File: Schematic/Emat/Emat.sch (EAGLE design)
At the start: 32 parts, among them J1 PIN1-2, J2 PIN1-2, J3 PIN1-2, J4 PIN1-2, Q2 STP13NM60N, U1 UCC27324D, X1 SMA-J502-ND

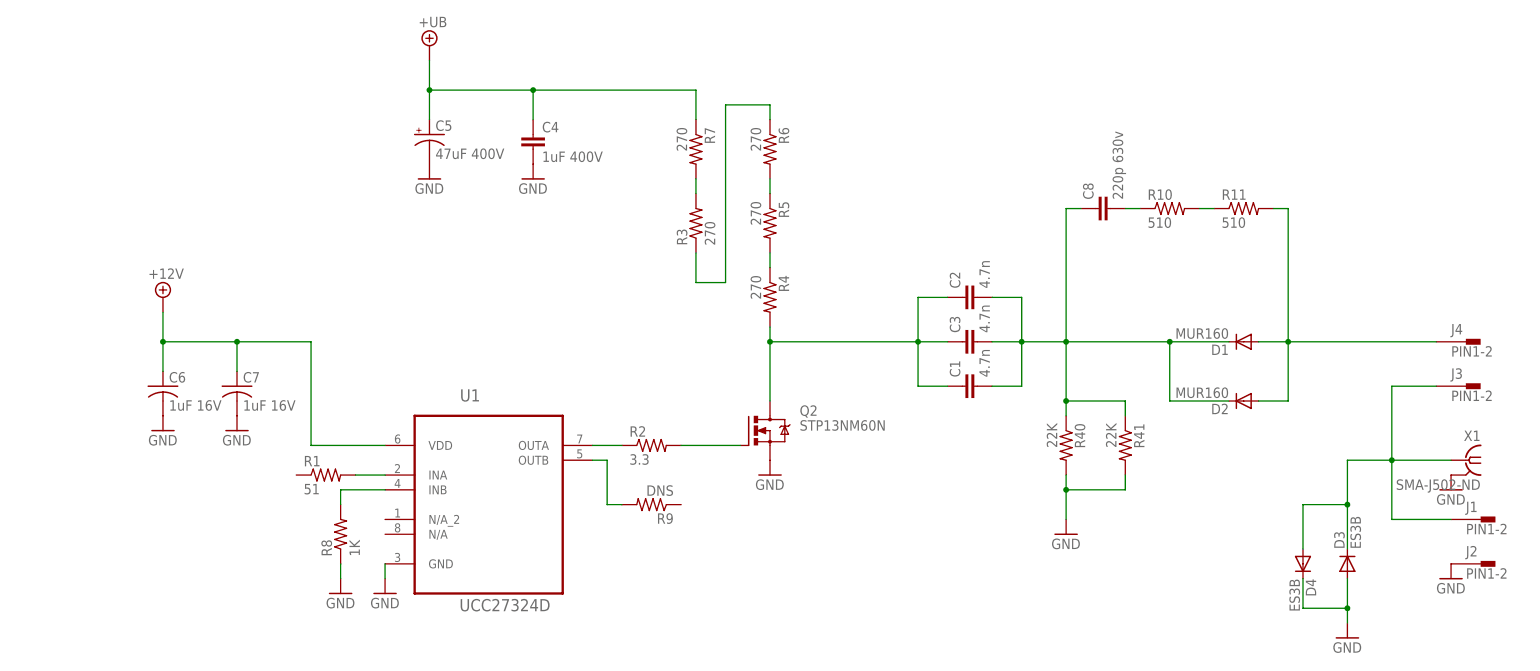
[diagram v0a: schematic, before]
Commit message: HV Key schematic done.
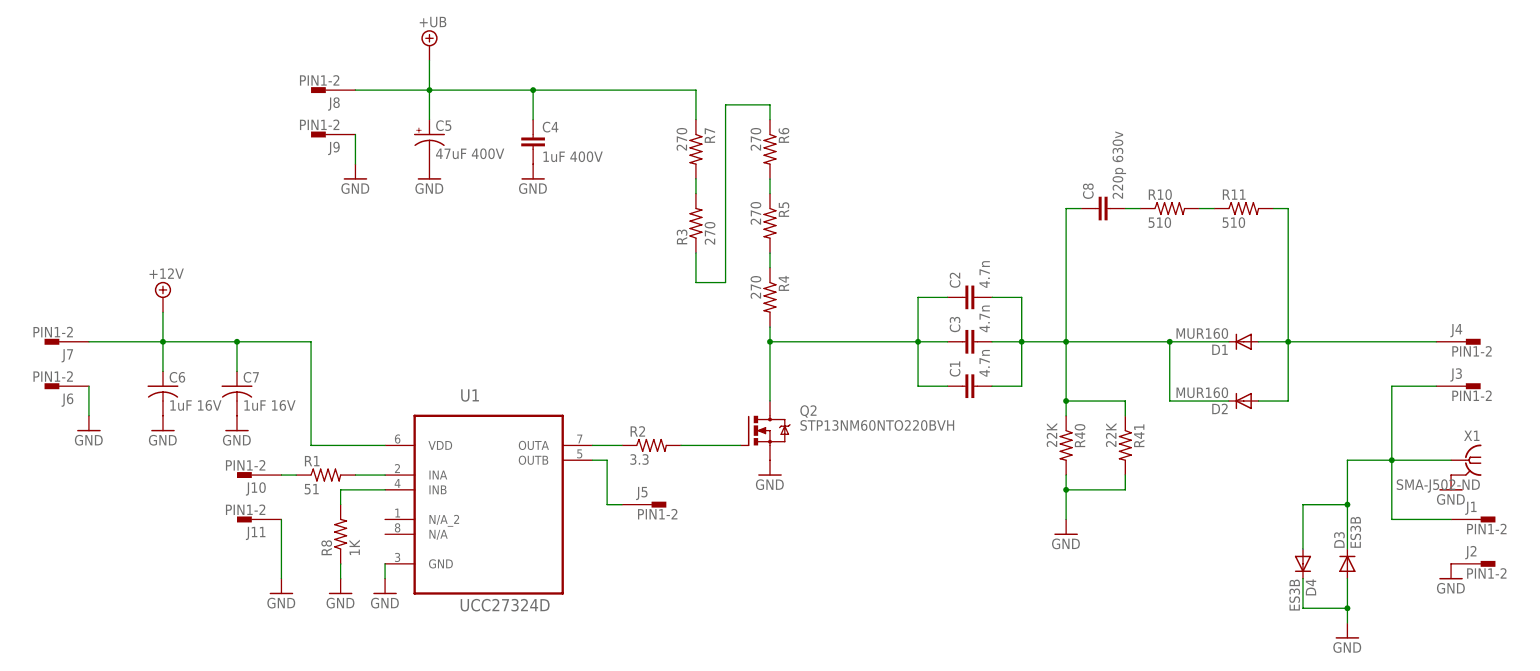
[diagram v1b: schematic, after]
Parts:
- removed R9: DNS, rcl:R-US_R1206
- added J10, J11, J5, J6, J7, J8, J9: PIN1-2, con-faston:PIN1-2
- Q2: value STP13NM60N -> STP13NM60NTO220BVH; device transistor-power:STP13NM60N -> transistor-power:STP13NM60NTO220BVH
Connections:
- new net N$5: J10.1, R1.1
- net +12V: now also J7.1
- net +UB: now also J8.1
- net GND: now also J11.1, J6.1, J9.1
- net N$12: now also J5.1; no longer R9.2
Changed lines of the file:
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@@
 <part name="R1" library="rcl" deviceset="R-US_" device="R1206" value="51"/>
 <part name="R2" library="rcl" deviceset="R-US_" device="R1206" value="3.3"/>
-<part name="Q2" library="transistor-power" deviceset="STP13NM60N" device=""/>
+<part name="Q2" library="transistor-power" deviceset="STP13NM60N" device="TO220BVH" value="STP13NM60NTO220BVH"/>
 <part name="R40" library="rcl" deviceset="R-US_" device="R2512" value="22K"/>
 <part name="R41" library="rcl" deviceset="R-US_" device="R2512" value="22K"/>
@@
 <part name="R8" library="rcl" deviceset="R-US_" device="R1206" value="1K"/>
 <part name="GND6" library="supply1" deviceset="GND" device=""/>
-<part name="R9" library="rcl" deviceset="R-US_" device="R1206" value="DNS"/>
 <part name="C6" library="rcl" deviceset="C-US" device="C0805" value="1uF 16V"/>
 <part name="C7" library="rcl" deviceset="C-US" device="C0805" value="1uF 16V"/>
@@
 <part name="J3" library="con-faston" deviceset="PIN1-2" device=""/>
 <part name="J4" library="con-faston" deviceset="PIN1-2" device=""/>
+<part name="J5" library="con-faston" deviceset="PIN1-2" device=""/>
+<part name="J6" library="con-faston" deviceset="PIN1-2" device=""/>
+<part name="J7" library="con-faston" deviceset="PIN1-2" device=""/>
+<part name="GND12" library="supply1" deviceset="GND" device=""/>
+<part name="J8" library="con-faston" deviceset="PIN1-2" device=""/>
+<part name="J9" library="con-faston" deviceset="PIN1-2" device=""/>
+<part name="GND13" library="supply1" deviceset="GND" device=""/>
+<part name="J10" library="con-faston" deviceset="PIN1-2" device=""/>
+<part name="J11" library="con-faston" deviceset="PIN1-2" device=""/>
+<part name="GND14" library="supply1" deviceset="GND" device=""/>
 </parts>
 <sheets>
@@
 <instance part="R8" gate="G$1" x="-5.08" y="55.88" rot="R90"/>
 <instance part="GND6" gate="1" x="-5.08" y="45.72"/>
-<instance part="R9" gate="G$1" x="48.26" y="60.96" rot="R180"/>
 <instance part="C6" gate="G$1" x="-35.56" y="81.28"/>
 <instance part="C7" gate="G$1" x="-22.86" y="81.28"/>
@@
 <instance part="J3" gate="G$1" x="187.96" y="81.28"/>
 <instance part="J4" gate="G$1" x="187.96" y="88.9"/>
+<instance part="J5" gate="G$1" x="48.26" y="60.96"/>
+<instance part="J6" gate="G$1" x="-53.34" y="81.28" rot="R180"/>
+<instance part="J7" gate="G$1" x="-53.34" y="88.9" rot="R180"/>
+<instance part="GND12" gate="1" x="-48.26" y="73.66"/>
+<instance part="J8" gate="G$1" x="-7.62" y="132.08" rot="R180"/>
+<instance part="J9" gate="G$1" x="-7.62" y="124.46" rot="R180"/>
+<instance part="GND13" gate="1" x="-2.54" y="116.84"/>
+<instance part="J10" gate="G$1" x="-20.32" y="66.04" rot="R180"/>
+<instance part="J11" gate="G$1" x="-20.32" y="58.42" rot="R180"/>
+<instance part="GND14" gate="1" x="-15.24" y="45.72"/>
 </instances>
 <busses>
@@
 <junction x="167.64" y="43.18"/>
 </segment>
+<segment>
+<pinref part="J6" gate="G$1" pin="1"/>
+<pinref part="GND12" gate="1" pin="GND"/>
+<wire x1="-48.26" y1="76.2" x2="-48.26" y2="81.28" width="0.1524" layer="91"/>
+</segment>
+<segment>
+<pinref part="J9" gate="G$1" pin="1"/>
+<pinref part="GND13" gate="1" pin="GND"/>
+<wire x1="-2.54" y1="119.38" x2="-2.54" y2="124.46" width="0.1524" layer="91"/>
+</segment>
+<segment>
+<pinref part="J11" gate="G$1" pin="1"/>
+<pinref part="GND14" gate="1" pin="GND"/>
+<wire x1="-15.24" y1="48.26" x2="-15.24" y2="58.42" width="0.1524" layer="91"/>
+</segment>
 </net>
 <net name="N$6" class="0">
@@
 <wire x1="38.1" y1="68.58" x2="40.64" y2="68.58" width="0.1524" layer="91"/>
 <wire x1="40.64" y1="68.58" x2="40.64" y2="60.96" width="0.1524" layer="91"/>
-<pinref part="R9" gate="G$1" pin="2"/>
 <wire x1="40.64" y1="60.96" x2="43.18" y2="60.96" width="0.1524" layer="91"/>
+<pinref part="J5" gate="G$1" pin="1"/>
 </segment>
 </net>
@@
 <wire x1="-35.56" y1="93.98" x2="-35.56" y2="88.9" width="0.1524" layer="91"/>
 <junction x="-35.56" y="88.9"/>
+<pinref part="J7" gate="G$1" pin="1"/>
+<wire x1="-48.26" y1="88.9" x2="-35.56" y2="88.9" width="0.1524" layer="91"/>
 </segment>
 </net>
@@
 <wire x1="10.16" y1="137.16" x2="10.16" y2="132.08" width="0.1524" layer="91"/>
 <junction x="10.16" y="132.08"/>
+<pinref part="J8" gate="G$1" pin="1"/>
+<wire x1="-2.54" y1="132.08" x2="10.16" y2="132.08" width="0.1524" layer="91"/>
 </segment>
 </net>
@@
 </segment>
 </net>
+<net name="N$5" class="0">
+<segment>
+<pinref part="R1" gate="G$1" pin="1"/>
+<pinref part="J10" gate="G$1" pin="1"/>
+<wire x1="-15.24" y1="66.04" x2="-12.7" y2="66.04" width="0.1524" layer="91"/>
+</segment>
+</net>

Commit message: Further work on schematic.
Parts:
- removed C8: 220p 630v, rcl:C-EUC1206K
- added C9: 220pF 1000V, rcl:C-EU075-042X103
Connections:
- net N$13: now also C9.2; no longer C8.2
- net N$16: now also C9.1; no longer C8.1
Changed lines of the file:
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@@
 <part name="GND8" library="supply1" deviceset="GND" device=""/>
 <part name="SUPPLY3" library="supply2" deviceset="+12V" device=""/>
-<part name="C8" library="rcl" deviceset="C-EU" device="C1206K" value="220p 630v"/>
 <part name="R10" library="rcl" deviceset="R-US_" device="R1206" value="510"/>
 <part name="R11" library="rcl" deviceset="R-US_" device="R1206" value="510"/>
@@
 <part name="J11" library="con-faston" deviceset="PIN1-2" device=""/>
 <part name="GND14" library="supply1" deviceset="GND" device=""/>
+<part name="C9" library="rcl" deviceset="C-EU" device="075-042X103" value="220pF 1000V"/>
 </parts>
 <sheets>
@@
 <instance part="GND8" gate="1" x="-35.56" y="73.66"/>
 <instance part="SUPPLY3" gate="+12V" x="-35.56" y="96.52"/>
-<instance part="C8" gate="G$1" x="124.46" y="111.76" rot="R90"/>
 <instance part="R10" gate="G$1" x="137.16" y="111.76"/>
 <instance part="R11" gate="G$1" x="149.86" y="111.76"/>
@@
 <instance part="J11" gate="G$1" x="-20.32" y="58.42" rot="R180"/>
 <instance part="GND14" gate="1" x="-15.24" y="45.72"/>
+<instance part="C9" gate="G$1" x="124.46" y="111.76" rot="R90"/>
 </instances>
 <busses>
@@
 <net name="N$13" class="0">
 <segment>
-<pinref part="C8" gate="G$1" pin="2"/>
 <pinref part="R10" gate="G$1" pin="1"/>
 <wire x1="129.54" y1="111.76" x2="132.08" y2="111.76" width="0.1524" layer="91"/>
+<pinref part="C9" gate="G$1" pin="2"/>
 </segment>
 </net>
@@
 <net name="N$16" class="0">
 <segment>
-<pinref part="C8" gate="G$1" pin="1"/>
 <wire x1="121.92" y1="111.76" x2="119.38" y2="111.76" width="0.1524" layer="91"/>
 <pinref part="C2" gate="G$1" pin="2"/>
@@
 <junction x="119.38" y="88.9"/>
 <wire x1="119.38" y1="111.76" x2="119.38" y2="88.9" width="0.1524" layer="91"/>
-</segment>
-</net>
+<pinref part="C9" gate="G$1" pin="1"/>
+</segment>
+</net>

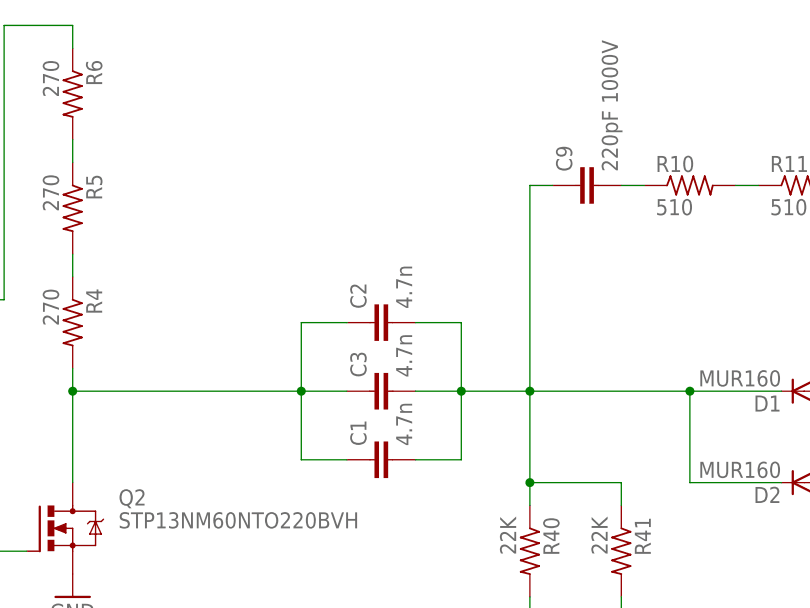
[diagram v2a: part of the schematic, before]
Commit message: 300V PCB modified, BOM added.
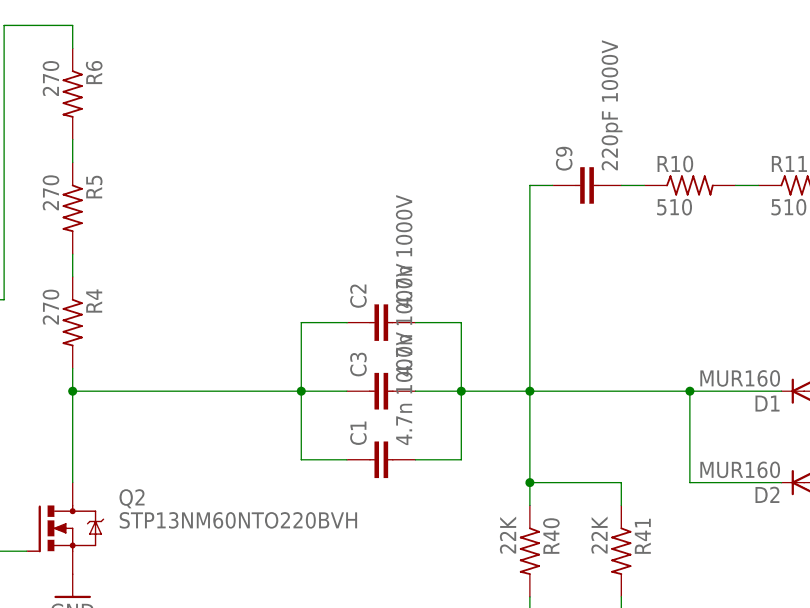
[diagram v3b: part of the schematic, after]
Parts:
- C1, C2, C3: value 4.7n -> 4.7n 1000V
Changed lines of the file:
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@@
 <part name="R40" library="rcl" deviceset="R-US_" device="R2512" value="22K"/>
 <part name="R41" library="rcl" deviceset="R-US_" device="R2512" value="22K"/>
-<part name="C1" library="capacitor-wima" deviceset="C" device="10/4" value="4.7n"/>
-<part name="C2" library="capacitor-wima" deviceset="C" device="10/4" value="4.7n"/>
-<part name="C3" library="capacitor-wima" deviceset="C" device="10/4" value="4.7n"/>
+<part name="C1" library="capacitor-wima" deviceset="C" device="10/4" value="4.7n 1000V"/>
+<part name="C2" library="capacitor-wima" deviceset="C" device="10/4" value="4.7n 1000V"/>
+<part name="C3" library="capacitor-wima" deviceset="C" device="10/4" value="4.7n 1000V"/>
 <part name="GND1" library="supply1" deviceset="GND" device=""/>
 <part name="D1" library="diode" deviceset="MUR160" device=""/>
